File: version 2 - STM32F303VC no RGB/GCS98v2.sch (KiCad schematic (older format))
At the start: 2 parts, among them U1 STM32F303CCTx

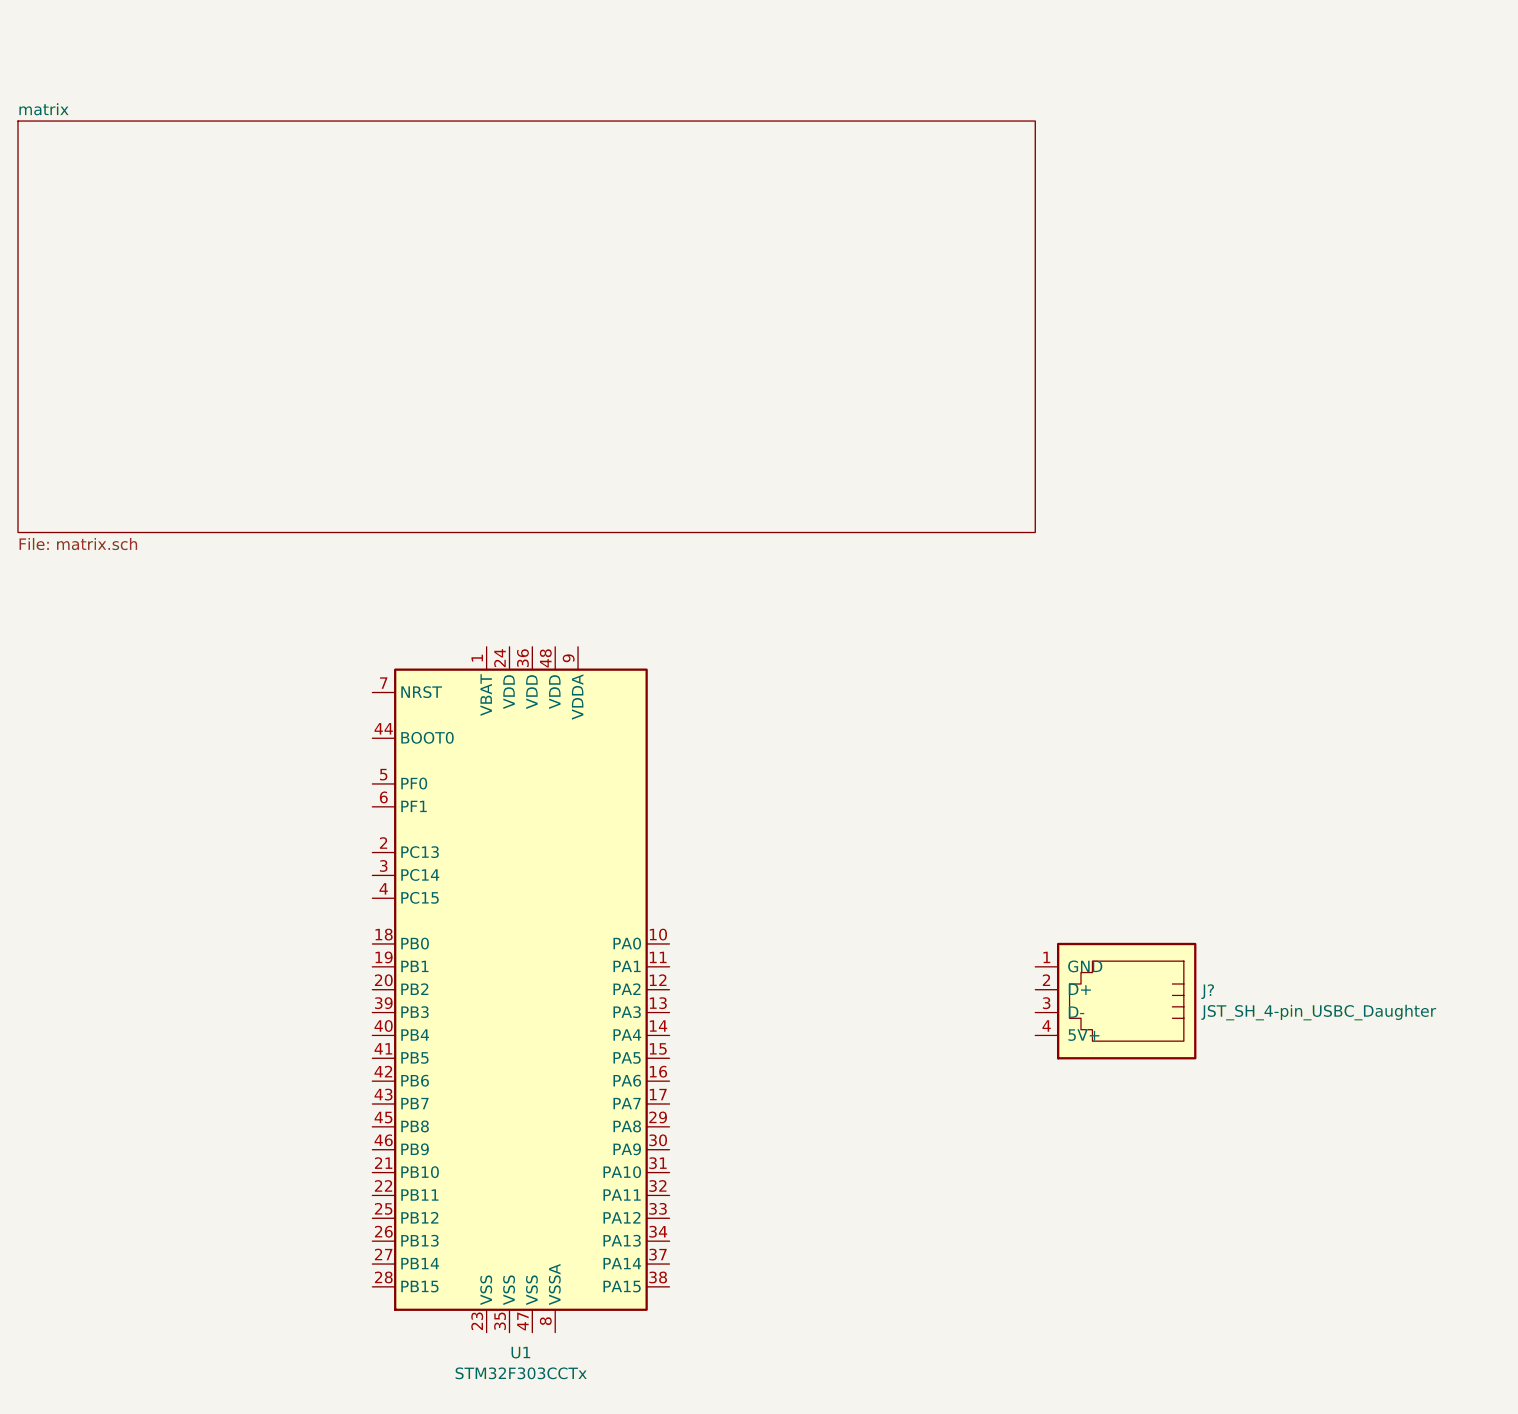
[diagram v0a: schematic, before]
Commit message: switch and diode layout done
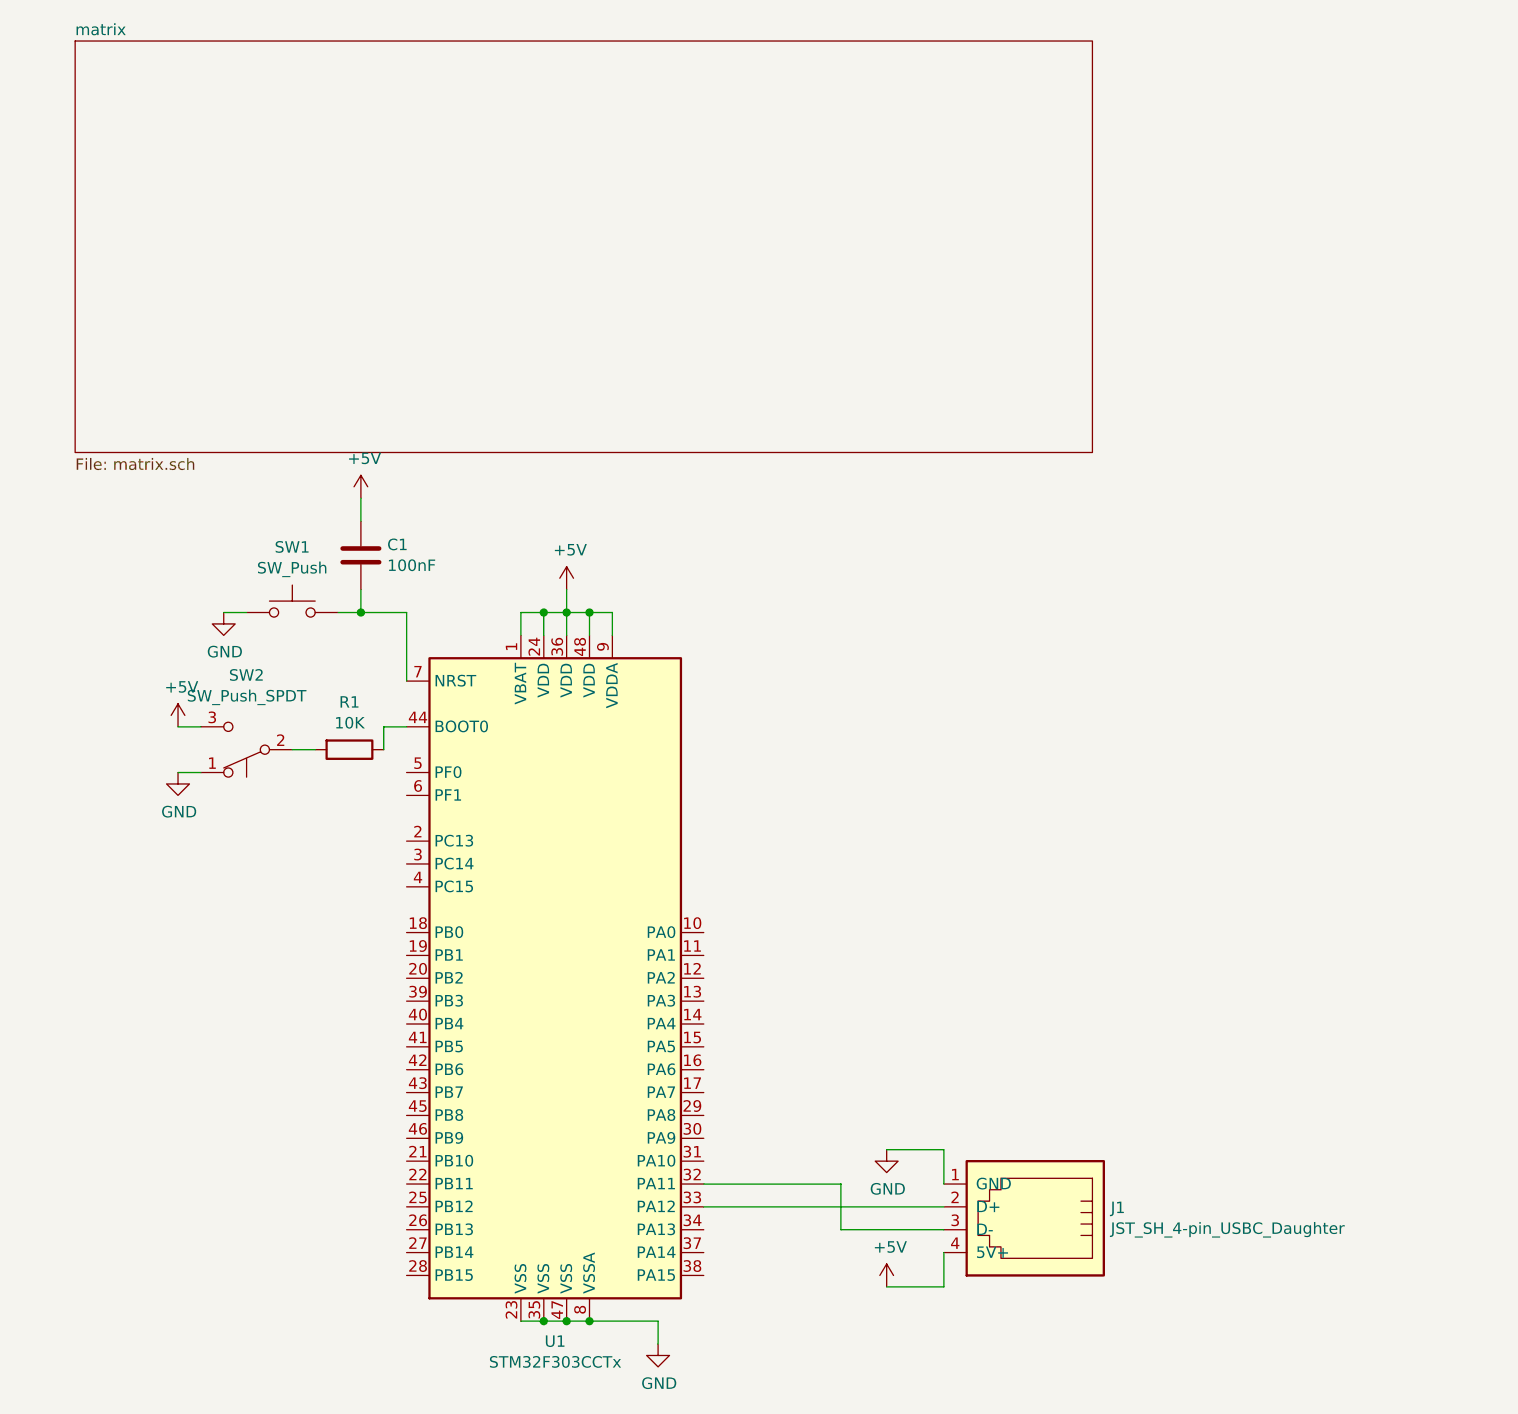
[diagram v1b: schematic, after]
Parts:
- added C1: 100nF, Capacitor_SMD:C_0805_2012Metric, symbol Device:C
- added R1: 10K, Resistor_SMD:R_0805_2012Metric, symbol Device:R
- added SW1: SW_Push, Button_Switch_SMD:SW_SPST_SKQG_WithStem, symbol Switch:SW_Push
- added SW2: SW_Push_SPDT, Button_Switch_SMD:SW_SPST_SKQG_WithStem, symbol Switch:SW_Push_SPDT
- gave numbers to parts that had none: 1
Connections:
- net +5V: now reaches U1.1 (VBAT)
- net +5V: now also J1.4 (5V+), U1.24 (VDD), U1.36 (VDD), U1.48 (VDD), U1.9 (VDDA), C1.1, SW2.3 (C)
- net GND: now reaches U1.23 (VSS)
- net GND: now also J1.1 (GND), U1.35 (VSS), U1.47 (VSS), U1.8 (VSSA), SW1.1, SW2.1 (A)
- net at U1.32 (PA11): now also J1.3 (D-)
- net at U1.33 (PA12): now also J1.2 (D+)
- net at U1.44 (BOOT0): now also R1.1
- net at U1.7 (NRST): now also C1.2, SW1.2
- new net: R1.2, SW2.2 (B)
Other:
- moved on the sheet: J1
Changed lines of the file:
@@
 $EndDescr
 $Sheet
-S 3450 950  4450 1800
+S 3700 600  4450 1800
 U 610059F7
 F0 "matrix" 50
@@
 $EndSheet
 $Comp
+L custom:JST_SH_4-pin_USBC_Daughter J1
+U 1 1 6100A588
+P 7900 5700
+F 0 "J1" H 7570 5704 50  0000 R CNN
+F 1 "JST_SH_4-pin_USBC_Daughter" H 7570 5795 50  0000 R CNN
+F 2 "" V 7900 5750 50  0001 C CNN
+F 3 "~" V 7900 5750 50  0001 C CNN
+	1    7900 5700
+	-1   0    0    1
+$EndComp
+$Comp
 L MCU_ST_STM32F3:STM32F303CCTx U1
-U 1 1 60FEA1D8
-P 5700 4750
-F 0 "U1" H 5650 3161 50  0000 C CNN
-F 1 "STM32F303CCTx" H 5650 3070 50  0000 C CNN
-F 2 "Package_QFP:LQFP-48_7x7mm_P0.5mm" H 5100 3350 50  0001 R CNN
-F 3 "http://www.st.com/st-web-ui/static/active/en/resource/technical/document/datasheet/DM00058181.pdf" H 5700 4750 50  0001 C CNN
-	1    5700 4750
-	1    0    0    -1
-$EndComp
-$Comp
-L custom:JST_SH_4-pin_USBC_Daughter J?
-U 1 1 6100A588
-P 8300 4750
-F 0 "J?" H 7970 4754 50  0000 R CNN
-F 1 "JST_SH_4-pin_USBC_Daughter" H 7970 4845 50  0000 R CNN
-F 2 "" V 8300 4800 50  0001 C CNN
-F 3 "~" V 8300 4800 50  0001 C CNN
-	1    8300 4750
+U 1 1 6100CAA2
+P 5850 4700
+F 0 "U1" H 5800 3111 50  0000 C CNN
+F 1 "STM32F303CCTx" H 5800 3020 50  0000 C CNN
+F 2 "Package_QFP:LQFP-48_7x7mm_P0.5mm" H 5250 3300 50  0001 R CNN
+F 3 "http://www.st.com/st-web-ui/static/active/en/resource/technical/document/datasheet/DM00058181.pdf" H 5850 4700 50  0001 C CNN
+	1    5850 4700
+	1    0    0    -1
+$EndComp
+Wire Wire Line
+	7500 5700 6450 5700
+Wire Wire Line
+	7500 5800 7050 5800
+Wire Wire Line
+	7050 5800 7050 5600
+Wire Wire Line
+	7050 5600 6450 5600
+$Comp
+L power:+5V #PWR0101
+U 1 1 61013A0D
+P 7250 6050
+F 0 "#PWR0101" H 7250 5900 50  0001 C CNN
+F 1 "+5V" H 7265 6223 50  0000 C CNN
+F 2 "" H 7250 6050 50  0001 C CNN
+F 3 "" H 7250 6050 50  0001 C CNN
+	1    7250 6050
+	1    0    0    -1
+$EndComp
+$Comp
+L power:GND #PWR0102
+U 1 1 610169D4
+P 7250 5450
+F 0 "#PWR0102" H 7250 5200 50  0001 C CNN
+F 1 "GND" H 7255 5277 50  0000 C CNN
+F 2 "" H 7250 5450 50  0001 C CNN
+F 3 "" H 7250 5450 50  0001 C CNN
+	1    7250 5450
+	1    0    0    -1
+$EndComp
+Wire Wire Line
+	7500 5600 7500 5450
+Wire Wire Line
+	7500 5450 7250 5450
+Wire Wire Line
+	7500 5900 7500 6050
+Wire Wire Line
+	7500 6050 7250 6050
+$Comp
+L power:+5V #PWR0103
+U 1 1 61018137
+P 5850 3000
+F 0 "#PWR0103" H 5850 2850 50  0001 C CNN
+F 1 "+5V" H 5865 3173 50  0000 C CNN
+F 2 "" H 5850 3000 50  0001 C CNN
+F 3 "" H 5850 3000 50  0001 C CNN
+	1    5850 3000
+	1    0    0    -1
+$EndComp
+Wire Wire Line
+	5650 3100 5650 3200
+Wire Wire Line
+	5750 3200 5750 3100
+Wire Wire Line
+	5850 3200 5850 3100
+Wire Wire Line
+	5950 3200 5950 3100
+Wire Wire Line
+	6050 3200 6050 3100
+Wire Wire Line
+	6050 3100 5950 3100
+Wire Wire Line
+	5950 3100 5850 3100
+Connection ~ 5950 3100
+Wire Wire Line
+	5750 3100 5850 3100
+Connection ~ 5850 3100
+Wire Wire Line
+	5750 3100 5650 3100
+Connection ~ 5750 3100
+Wire Wire Line
+	5850 3100 5850 3000
+$Comp
+L power:GND #PWR0104
+U 1 1 6101ADDA
+P 6250 6300
+F 0 "#PWR0104" H 6250 6050 50  0001 C CNN
+F 1 "GND" H 6255 6127 50  0000 C CNN
+F 2 "" H 6250 6300 50  0001 C CNN
+F 3 "" H 6250 6300 50  0001 C CNN
+	1    6250 6300
+	1    0    0    -1
+$EndComp
+Wire Wire Line
+	5650 6200 5750 6200
+Wire Wire Line
+	5750 6200 5850 6200
+Connection ~ 5750 6200
+Wire Wire Line
+	5850 6200 5950 6200
+Connection ~ 5850 6200
+Wire Wire Line
+	5950 6200 6250 6200
+Connection ~ 5950 6200
+Wire Wire Line
+	6250 6200 6250 6300
+$Comp
+L Switch:SW_Push SW1
+U 1 1 6102940B
+P 4650 3100
+F 0 "SW1" H 4650 3385 50  0000 C CNN
+F 1 "SW_Push" H 4650 3294 50  0000 C CNN
+F 2 "Button_Switch_SMD:SW_SPST_SKQG_WithStem" H 4650 3300 50  0001 C CNN
+F 3 "~" H 4650 3300 50  0001 C CNN
+	1    4650 3100
+	1    0    0    -1
+$EndComp
+$Comp
+L power:GND #PWR0105
+U 1 1 6102B40E
+P 4350 3100
+F 0 "#PWR0105" H 4350 2850 50  0001 C CNN
+F 1 "GND" H 4355 2927 50  0000 C CNN
+F 2 "" H 4350 3100 50  0001 C CNN
+F 3 "" H 4350 3100 50  0001 C CNN
+	1    4350 3100
+	1    0    0    -1
+$EndComp
+$Comp
+L power:+5V #PWR0106
+U 1 1 6102D70A
+P 4950 2600
+F 0 "#PWR0106" H 4950 2450 50  0001 C CNN
+F 1 "+5V" H 4965 2773 50  0000 C CNN
+F 2 "" H 4950 2600 50  0001 C CNN
+F 3 "" H 4950 2600 50  0001 C CNN
+	1    4950 2600
+	1    0    0    -1
+$EndComp
+Wire Wire Line
+	4350 3100 4450 3100
+Wire Wire Line
+	4950 2600 4950 2700
+Wire Wire Line
+	4950 3000 4950 3100
+$Comp
+L Device:C C1
+U 1 1 6103C47B
+P 4950 2850
+F 0 "C1" H 5065 2896 50  0000 L CNN
+F 1 "100nF" H 5065 2805 50  0000 L CNN
+F 2 "Capacitor_SMD:C_0805_2012Metric" H 4988 2700 50  0001 C CNN
+F 3 "~" H 4950 2850 50  0001 C CNN
+	1    4950 2850
+	1    0    0    -1
+$EndComp
+$Comp
+L Device:R R1
+U 1 1 6103CF3B
+P 4900 3700
+F 0 "R1" V 4693 3700 50  0000 C CNN
+F 1 "10K" V 4784 3700 50  0000 C CNN
+F 2 "Resistor_SMD:R_0805_2012Metric" V 4830 3700 50  0001 C CNN
+F 3 "~" H 4900 3700 50  0001 C CNN
+	1    4900 3700
+	0    1    1    0
+$EndComp
+$Comp
+L Switch:SW_Push_SPDT SW2
+U 1 1 610400A2
+P 4450 3700
+F 0 "SW2" H 4450 3375 50  0000 C CNN
+F 1 "SW_Push_SPDT" H 4450 3466 50  0000 C CNN
+F 2 "Button_Switch_SMD:SW_SPST_SKQG_WithStem" H 4450 3700 50  0001 C CNN
+F 3 "~" H 4450 3700 50  0001 C CNN
+	1    4450 3700
 	-1   0    0    1
 $EndComp
+$Comp
+L power:+5V #PWR0107
+U 1 1 61044F33
+P 4150 3600
+F 0 "#PWR0107" H 4150 3450 50  0001 C CNN
+F 1 "+5V" H 4165 3773 50  0000 C CNN
+F 2 "" H 4150 3600 50  0001 C CNN
+F 3 "" H 4150 3600 50  0001 C CNN
+	1    4150 3600
+	1    0    0    -1
+$EndComp
+$Comp
+L power:GND #PWR0108
+U 1 1 61045EAD
+P 4150 3800
+F 0 "#PWR0108" H 4150 3550 50  0001 C CNN
+F 1 "GND" H 4155 3627 50  0000 C CNN
+F 2 "" H 4150 3800 50  0001 C CNN
+F 3 "" H 4150 3800 50  0001 C CNN
+	1    4150 3800
+	1    0    0    -1
+$EndComp
+Wire Wire Line
+	4150 3600 4250 3600
+Wire Wire Line
+	4150 3800 4250 3800
+Wire Wire Line
+	4650 3700 4750 3700
+Wire Wire Line
+	5050 3600 5150 3600
+Wire Wire Line
+	4850 3100 4950 3100
+Connection ~ 4950 3100
+Wire Wire Line
+	4950 3100 5150 3100
+Wire Wire Line
+	5150 3100 5150 3400
+Wire Wire Line
+	5050 3600 5050 3700
 $EndSCHEMATC
